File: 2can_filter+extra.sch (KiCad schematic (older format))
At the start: 24 parts, among them J5 54819-0572, J6 NOT_FITTED_SWD_Conn_01x04_Male, U10 74HC4050D, U11 TJA1040T, U12 TJA1040T, U8 74HC4050D, U9 STM32F105RBTx, Y2 Crystal KX-13 25MHz

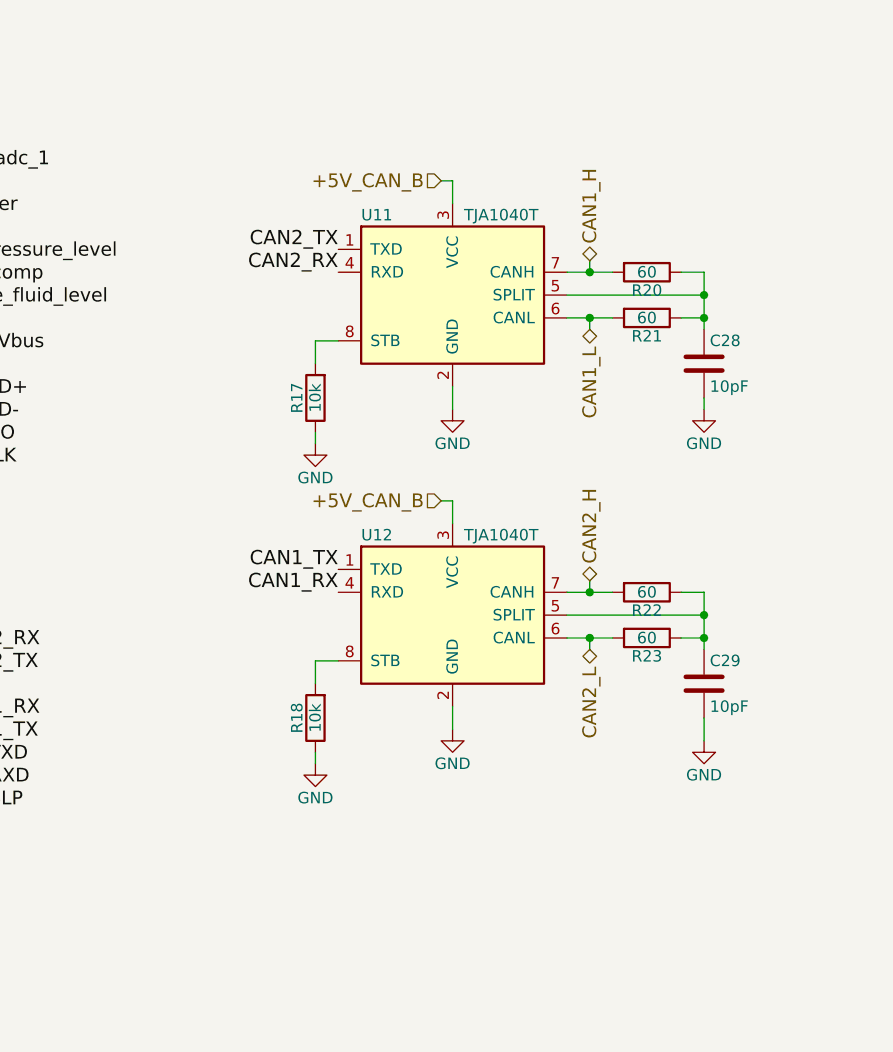
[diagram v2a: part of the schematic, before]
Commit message: add transient voltage suppression diods on CAN
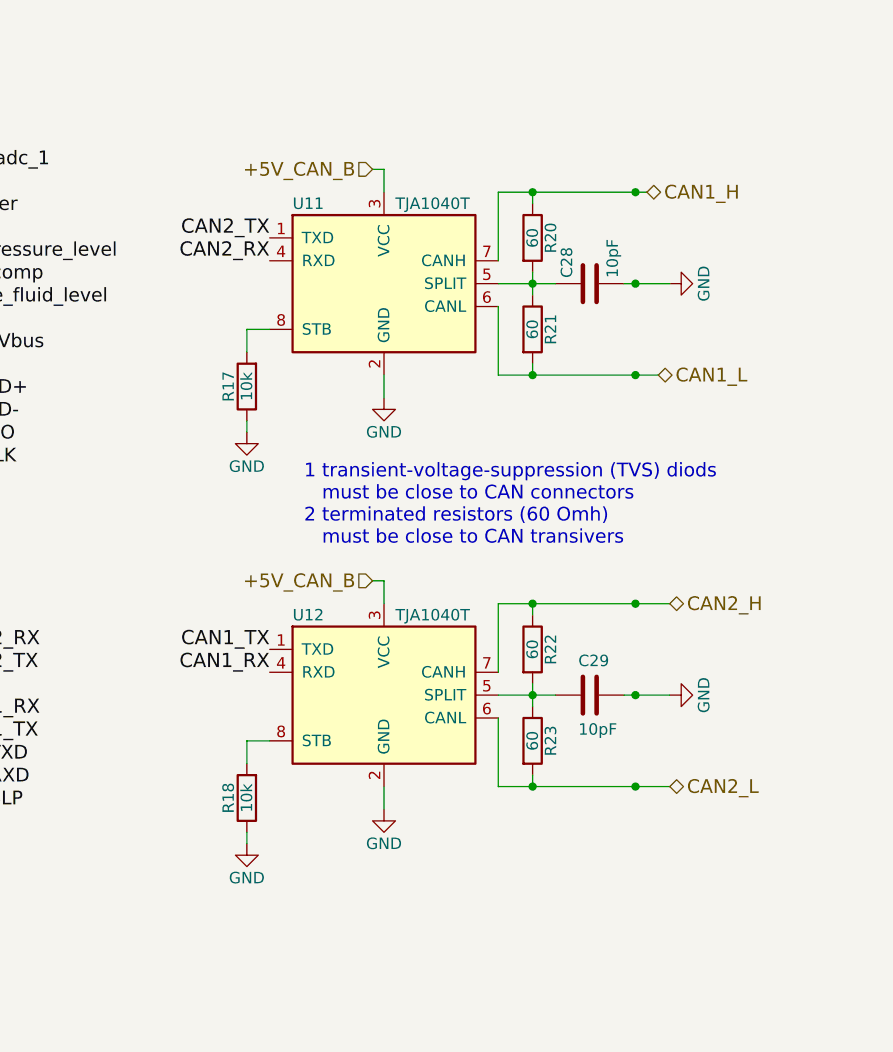
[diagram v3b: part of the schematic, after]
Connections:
- net CAN1_H: now also R20.1; no longer R20.2
- net CAN2_H: now also R22.1; no longer R22.2
- net GND: now also C29.1; no longer C29.2
- net at C28.1, R21.1, U11.5 (SPLIT): now also R20.2; no longer R20.1
- net at R23.1, U12.5 (SPLIT): now also C29.2, R22.2; no longer C29.1, R22.1
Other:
- note added: "1 transient-voltage-suppression (TVS) diods\n must be close to CAN connectors\n2 terminated resistors (60 Omh)\n must be close to CAN transivers"
- moved on the sheet: C28, C29, R17, R18, R20, R21, R22, R23, U11, U12

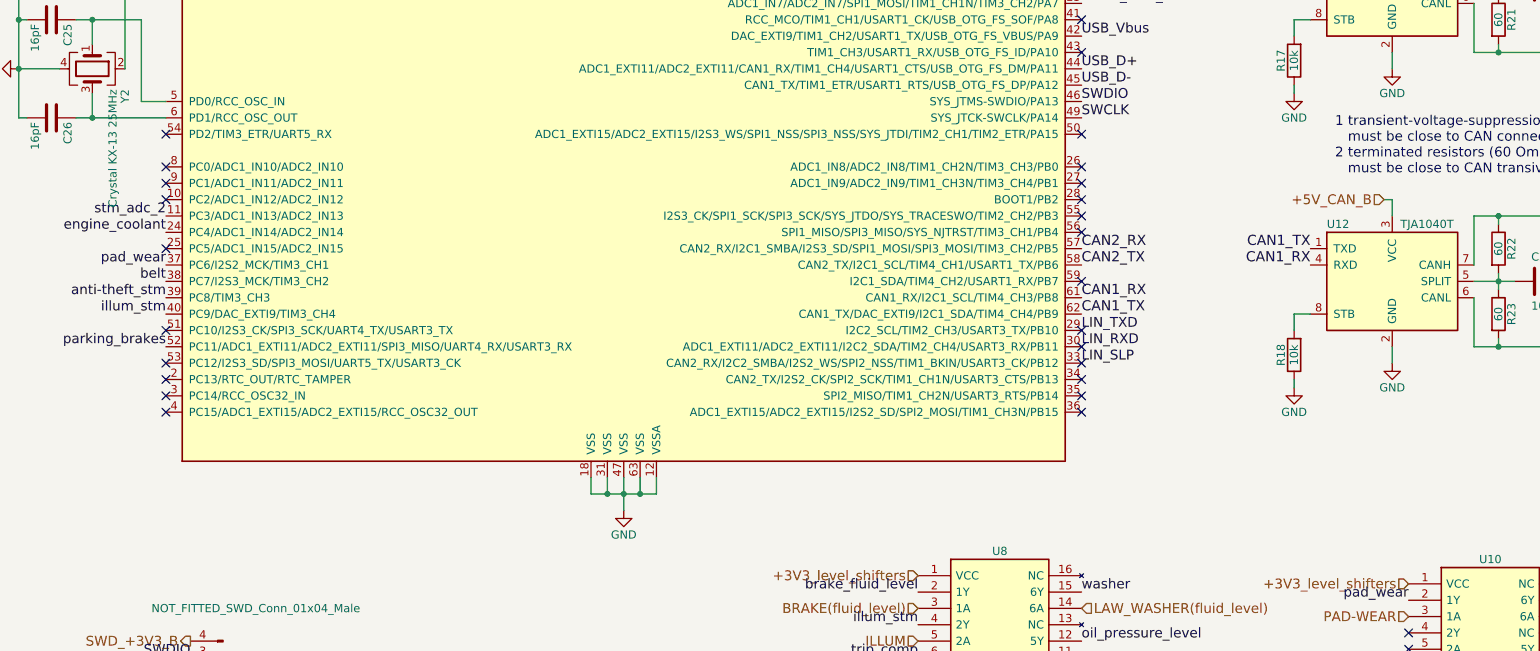
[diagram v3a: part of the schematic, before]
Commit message: sch&pcb: add LED`s and refresh readme image`s
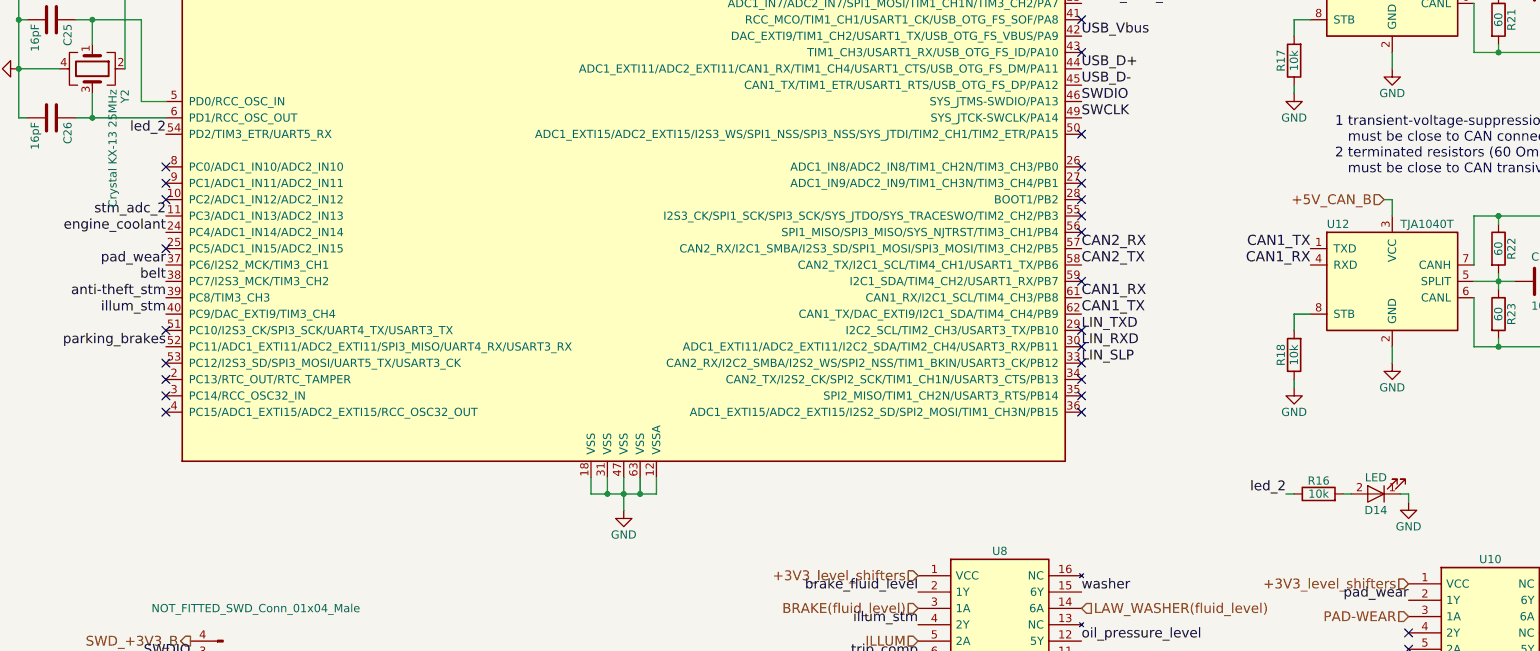
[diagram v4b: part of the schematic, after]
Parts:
- added D14: LED, LEDs:LED_0805, symbol LED
- added R16: 10k, Resistors_SMD:R_0805, symbol R
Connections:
- net GND: now also D14.1 (K)
- net led_2: now reaches U9.54 (PD2/TIM3_ETR/UART5_RX)
- net led_2: now also R16.1
- new net: D14.2 (A), R16.2
- no-connect marks 34 -> 33
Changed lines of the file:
@@
 	1250 7250 1500 7250
 $Comp
-L GND #PWR016
+L GND #PWR017
 U 1 1 5A047DA1
 P 1500 7250
-F 0 "#PWR016" H 1500 7000 50  0001 C CNN
+F 0 "#PWR017" H 1500 7000 50  0001 C CNN
 F 1 "GND" H 1500 7100 50  0000 C CNN
 F 2 "" H 1500 7250 50  0001 C CNN
@@
 Connection ~ 4500 4850
 $Comp
-L GND #PWR017
+L GND #PWR018
 U 1 1 5A0480FC
 P 4600 4950
-F 0 "#PWR017" H 4600 4700 50  0001 C CNN
+F 0 "#PWR018" H 4600 4700 50  0001 C CNN
 F 1 "GND" H 4600 4800 50  0000 C CNN
 F 2 "" H 4600 4950 50  0001 C CNN
@@
 	8700 2350 8700 2400
 $Comp
-L GND #PWR018
+L GND #PWR019
 U 1 1 5A09EB23
 P 9300 2250
-F 0 "#PWR018" H 9300 2000 50  0001 C CNN
+F 0 "#PWR019" H 9300 2000 50  0001 C CNN
 F 1 "GND" H 9300 2100 50  0000 C CNN
 F 2 "" H 9300 2250 50  0001 C CNN
@@
 	9300 2150 9300 2250
 $Comp
-L GND #PWR019
+L GND #PWR020
 U 1 1 5A048D93
 P 10550 1750
-F 0 "#PWR019" H 10550 1500 50  0001 C CNN
+F 0 "#PWR020" H 10550 1500 50  0001 C CNN
 F 1 "GND" H 10550 1600 50  0000 C CNN
 F 2 "" H 10550 1750 50  0001 C CNN
@@
 $EndComp
 $Comp
-L GND #PWR020
+L GND #PWR021
 U 1 1 5A048E0B
 P 8700 2400
-F 0 "#PWR020" H 8700 2150 50  0001 C CNN
+F 0 "#PWR021" H 8700 2150 50  0001 C CNN
 F 1 "GND" H 8700 2250 50  0000 C CNN
 F 2 "" H 8700 2400 50  0001 C CNN
@@
 	8700 4150 8700 4200
 $Comp
-L GND #PWR021
+L GND #PWR022
 U 1 1 5A048FA0
 P 8700 4200
-F 0 "#PWR021" H 8700 3950 50  0001 C CNN
+F 0 "#PWR022" H 8700 3950 50  0001 C CNN
 F 1 "GND" H 8700 4050 50  0000 C CNN
 F 2 "" H 8700 4200 50  0001 C CNN
@@
 $EndComp
 $Comp
-L GND #PWR022
+L GND #PWR023
 U 1 1 5A049172
 P 9300 4050
-F 0 "#PWR022" H 9300 3800 50  0001 C CNN
+F 0 "#PWR023" H 9300 3800 50  0001 C CNN
 F 1 "GND" H 9300 3900 50  0000 C CNN
 F 2 "" H 9300 4050 50  0001 C CNN
@@
 	9300 3950 9300 4050
 $Comp
-L GND #PWR023
+L GND #PWR024
 U 1 1 5A09EB29
 P 10550 3550
-F 0 "#PWR023" H 10550 3300 50  0001 C CNN
+F 0 "#PWR024" H 10550 3300 50  0001 C CNN
 F 1 "GND" H 10550 3400 50  0000 C CNN
 F 2 "" H 10550 3550 50  0001 C CNN
@@
 	1950 6200 1950 6050
 $Comp
-L GND #PWR024
+L GND #PWR025
 U 1 1 5A09EB2C
 P 1950 6200
-F 0 "#PWR024" H 1950 5950 50  0001 C CNN
+F 0 "#PWR025" H 1950 5950 50  0001 C CNN
 F 1 "GND" H 1950 6050 50  0000 C CNN
 F 2 "" H 1950 6200 50  0001 C CNN
@@
 $EndComp
 $Comp
-L GND #PWR025
+L GND #PWR026
 U 1 1 5A09EB31
 P 900 2250
-F 0 "#PWR025" H 900 2000 50  0001 C CNN
+F 0 "#PWR026" H 900 2000 50  0001 C CNN
 F 1 "GND" H 900 2100 50  0000 C CNN
 F 2 "" H 900 2250 50  0001 C CNN
@@
 Connection ~ 1350 2550
 $Comp
-L GND #PWR026
+L GND #PWR027
 U 1 1 5A09EB32
 P 4200 7300
-F 0 "#PWR026" H 4200 7050 50  0001 C CNN
+F 0 "#PWR027" H 4200 7050 50  0001 C CNN
 F 1 "GND" H 4200 7150 50  0000 C CNN
 F 2 "" H 4200 7300 50  0001 C CNN
@@
 Connection ~ 5750 7200
 $Comp
-L GND #PWR027
+L GND #PWR028
 U 1 1 5A09F076
 P 6200 7250
-F 0 "#PWR027" H 6200 7000 50  0001 C CNN
+F 0 "#PWR028" H 6200 7000 50  0001 C CNN
 F 1 "GND" H 6200 7100 50  0000 C CNN
 F 2 "" H 6200 7250 50  0001 C CNN
@@
 anti-theft_stm
 $Comp
-L GND #PWR028
+L GND #PWR029
 U 1 1 5A0A1F34
 P 6300 6150
-F 0 "#PWR028" H 6300 5900 50  0001 C CNN
+F 0 "#PWR029" H 6300 5900 50  0001 C CNN
 F 1 "GND" H 6300 6000 50  0000 C CNN
 F 2 "" H 6300 6150 50  0001 C CNN
@@
 NoConn ~ 1800 2950
 NoConn ~ 1800 2850
-NoConn ~ 1800 2650
 NoConn ~ 7400 1150
 NoConn ~ 7400 1350
@@
 Connection ~ 4200 7250
 $Comp
-L GND #PWR029
+L GND #PWR030
 U 1 1 5A0EC5D8
 P 9300 6250
-F 0 "#PWR029" H 9300 6000 50  0001 C CNN
+F 0 "#PWR030" H 9300 6000 50  0001 C CNN
 F 1 "GND" H 9300 6100 50  0000 C CNN
 F 2 "" H 9300 6250 50  0001 C CNN
@@
 Text Notes 8950 2900 0    60   ~ 0
 1 transient-voltage-suppression (TVS) diods\n   must be close to CAN connectors\n2 terminated resistors (60 Omh)\n   must be close to CAN transivers
+$Comp
+L R R16
+U 1 1 5A268E3F
+P 8850 4850
+F 0 "R16" V 8930 4850 50  0000 C CNN
+F 1 "10k" V 8850 4850 50  0000 C CNN
+F 2 "Resistors_SMD:R_0805" V 8780 4850 50  0001 C CNN
+F 3 "" H 8850 4850 50  0001 C CNN
+	1    8850 4850
+	0    -1   -1   0
+$EndComp
+$Comp
+L LED D14
+U 1 1 5A268EBD
+P 9200 4850
+F 0 "D14" H 9200 4950 50  0000 C CNN
+F 1 "LED" H 9200 4750 50  0000 C CNN
+F 2 "LEDs:LED_0805" H 9200 4850 50  0001 C CNN
+F 3 "" H 9200 4850 50  0001 C CNN
+	1    9200 4850
+	-1   0    0    1
+$EndComp
+$Comp
+L GND #PWR031
+U 1 1 5A268F34
+P 9400 4900
+F 0 "#PWR031" H 9400 4650 50  0001 C CNN
+F 1 "GND" H 9400 4750 50  0000 C CNN
+F 2 "" H 9400 4900 50  0001 C CNN
+F 3 "" H 9400 4900 50  0001 C CNN
+	1    9400 4900
+	1    0    0    -1
+$EndComp
+Wire Wire Line
+	9000 4850 9050 4850
+Wire Wire Line
+	9350 4850 9400 4850
+Wire Wire Line
+	9400 4850 9400 4900
+Wire Wire Line
+	8700 4850 8650 4850
+Text Label 8650 4850 2    60   ~ 0
+led_2
+Text Label 1800 2650 2    60   ~ 0
+led_2
 $EndSCHEMATC

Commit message: add usb 3d modele
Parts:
- J5: footprint zulljon:USB_mini_B -> zpkl:USB_mini_B
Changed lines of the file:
@@
 F 0 "J5" H 3600 7200 50  0000 C CNN
 F 1 "54819-0572" H 3600 6700 50  0000 C CNN
-F 2 "zulljon:USB_mini_B" H 3600 6600 50  0001 C CNN
+F 2 "zpkl:USB_mini_B" H 3600 6600 50  0001 C CNN
 F 3 "http://www.molex.com/webdocs/datasheets/pdf/en-us/0548190572_IO_CONNECTORS.pdf" H 3600 6500 50  0001 C CNN
 F 4 "Surface mount onthego connector,1A 30V Molex On-The-Go Series Right Angle SMT Version 2.0 Type B Mini USB Connector Receptacle, 30 V, 1A" H 3600 6400 50  0001 C CNN "Description"

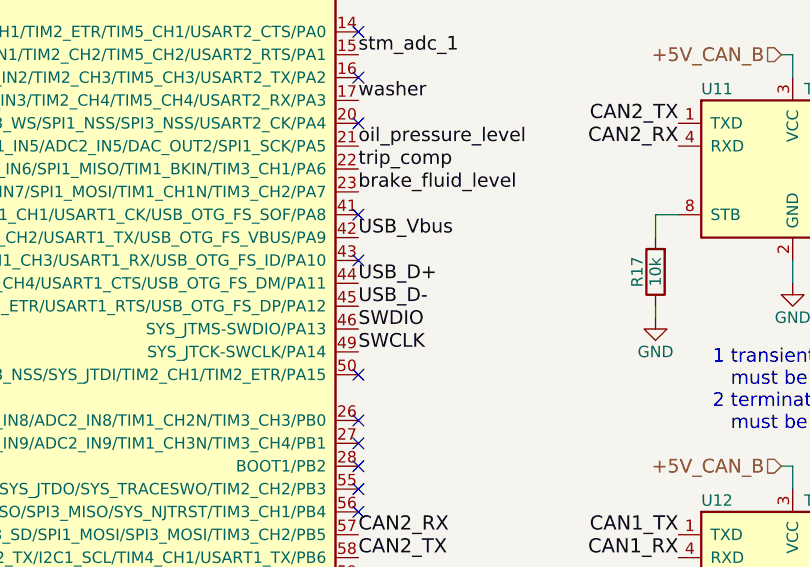
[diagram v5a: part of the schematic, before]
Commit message: fix USB, swapped the traces D+ D-
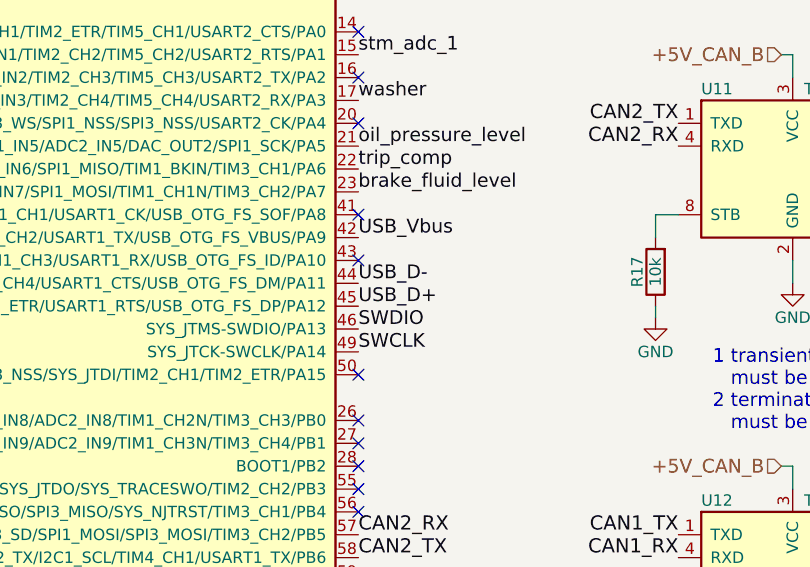
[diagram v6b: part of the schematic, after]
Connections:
- net USB_D+: now also U9.45 (CAN1_TX/TIM1_ETR/USART1_RTS/USB_OTG_FS_DP/PA12); no longer U9.44 (ADC1_EXTI11/ADC2_EXTI11/CAN1_RX/TIM1_CH4/USART1_CTS/USB_OTG_FS_DM/PA11)
- net USB_D-: now also U9.44 (ADC1_EXTI11/ADC2_EXTI11/CAN1_RX/TIM1_CH4/USART1_CTS/USB_OTG_FS_DM/PA11); no longer U9.45 (CAN1_TX/TIM1_ETR/USART1_RTS/USB_OTG_FS_DP/PA12)
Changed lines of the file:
@@
 Text Label 2500 7150 2    60   ~ 0
 USB_D-
+Text Label 7400 2350 0    60   ~ 0
+USB_D+
 Text Label 7400 2250 0    60   ~ 0
-USB_D+
-Text Label 7400 2350 0    60   ~ 0
 USB_D-
 Text HLabel 9250 3050 0    60   Input ~ 0

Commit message: fix CAN, swapped the stm->to->can connection in module B
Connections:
- net CAN1_H renamed CAN_HS_H
- net CAN1_L renamed CAN_HS_L
- net CAN1_RX renamed CAN_HS_RX
- net CAN_HS_RX: now also U11.4 (RXD); no longer U12.4 (RXD)
- net CAN1_TX renamed CAN_HS_TX
- net CAN_HS_TX: now also U11.1 (TXD); no longer U12.1 (TXD)
- net CAN2_H renamed CAN_MS_H
- net CAN2_L renamed CAN_MS_L
- net CAN2_RX renamed CAN_MS_RX
- net CAN_MS_RX: now also U12.4 (RXD); no longer U11.4 (RXD)
- net CAN2_TX renamed CAN_MS_TX
- net CAN_MS_TX: now also U12.1 (TXD); no longer U11.1 (TXD)
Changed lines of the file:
@@
 LIBS:valves
 LIBS:stm32
-LIBS:LM2596SX-5.0_NOPB
-LIBS:lm2575s-5
-LIBS:74HC4050D
-LIBS:54819-0572
+LIBS:zpkl
 LIBS:instrument_cluster-cache
 EELAYER 25 0
@@
 $EndComp
 Text HLabel 10450 1350 2    60   BiDi ~ 0
-CAN1_H
+CAN_HS_H
 Text HLabel 10500 2150 2    60   BiDi ~ 0
-CAN1_L
+CAN_HS_L
 Text HLabel 10550 3150 2    60   BiDi ~ 0
-CAN2_H
+CAN_MS_H
 Text HLabel 10550 3950 2    60   BiDi ~ 0
-CAN2_L
+CAN_MS_L
 $Comp
 L TJA1040T U12
@@
 NoConn ~ 1800 1150
 Text Label 7400 3350 0    62   ~ 0
-CAN2_RX
+CAN_MS_RX
 Text Label 7400 3450 0    62   ~ 0
-CAN2_TX
+CAN_MS_TX
 Text Label 7400 3650 0    62   ~ 0
-CAN1_RX
+CAN_HS_RX
 Text Label 7400 3750 0    62   ~ 0
-CAN1_TX
+CAN_HS_TX
+Text Label 8800 3450 2    62   ~ 0
+CAN_MS_RX
+Text Label 8800 3350 2    62   ~ 0
+CAN_MS_TX
 Text Label 8800 1650 2    62   ~ 0
-CAN2_RX
+CAN_HS_RX
 Text Label 8800 1550 2    62   ~ 0
-CAN2_TX
-Text Label 8800 3450 2    62   ~ 0
-CAN1_RX
-Text Label 8800 3350 2    62   ~ 0
-CAN1_TX
+CAN_HS_TX
 $Comp
 L 74HC4050D U10

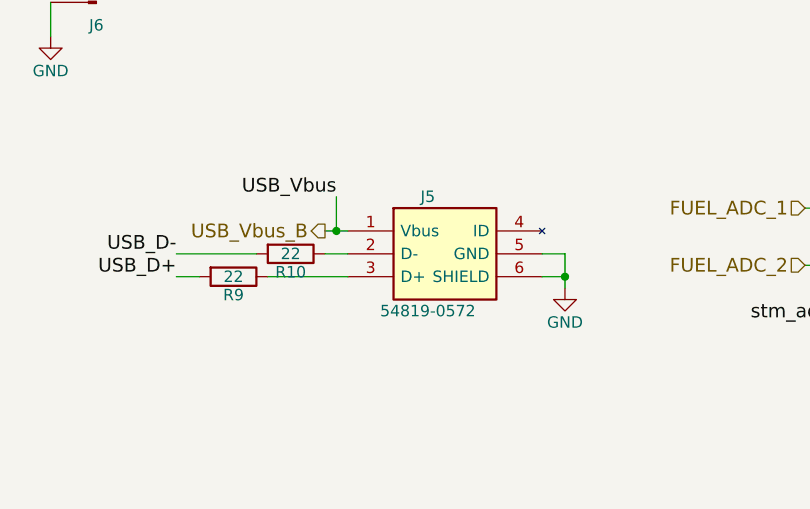
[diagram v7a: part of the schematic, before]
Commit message: fix USB footprint
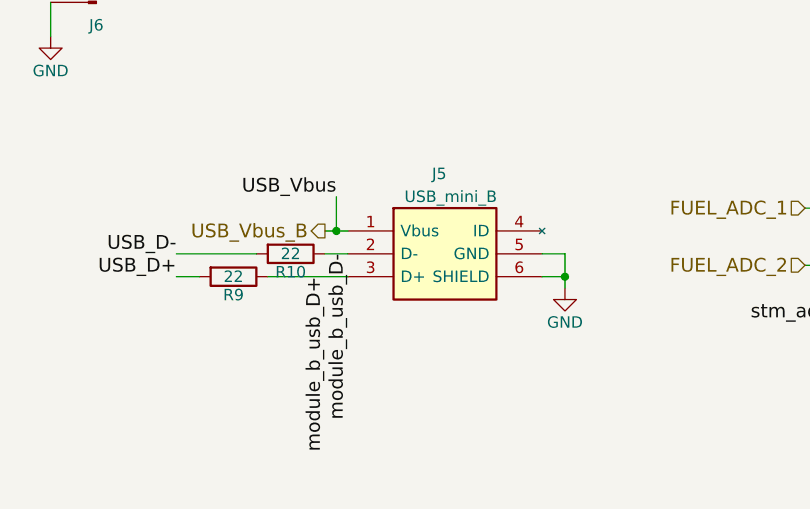
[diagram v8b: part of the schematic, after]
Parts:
- J5: value 54819-0572 -> USB_mini_B; footprint zpkl:USB_mini_B -> zpkl:USB-B-M5-SMD-C
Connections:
- net module_b_usb_D-: now reaches J5.2 (D-), R10.1
- net module_b_usb_D+: now reaches J5.3 (D+), R9.1
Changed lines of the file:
@@
 AR Path="/5A09AC68" Ref="J5"  Part="1"
 AR Path="/5A0472F5/5A09AC68" Ref="J5"  Part="1"
-F 0 "J5" H 3600 7200 50  0000 C CNN
-F 1 "54819-0572" H 3600 6700 50  0000 C CNN
-F 2 "zpkl:USB_mini_B" H 3600 6600 50  0001 C CNN
+F 0 "J5" H 3650 7300 50  0000 C CNN
+F 1 "USB_mini_B" H 3700 7200 50  0000 C CNN
+F 2 "zpkl:USB-B-M5-SMD-C" H 3600 6600 50  0001 C CNN
 F 3 "http://www.molex.com/webdocs/datasheets/pdf/en-us/0548190572_IO_CONNECTORS.pdf" H 3600 6500 50  0001 C CNN
 F 4 "Surface mount onthego connector,1A 30V Molex On-The-Go Series Right Angle SMT Version 2.0 Type B Mini USB Connector Receptacle, 30 V, 1A" H 3600 6400 50  0001 C CNN "Description"
@@
 Text Label 1800 2650 2    60   ~ 0
 led_2
+Text Label 3250 7150 3    60   ~ 0
+module_b_usb_D-
+Text Label 3150 7250 3    60   ~ 0
+module_b_usb_D+
 $EndSCHEMATC
